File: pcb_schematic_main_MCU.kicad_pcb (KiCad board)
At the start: 2 copper layers, 100.1 x 70.1 mm, 106 parts, among them IC1 LM76202QPWPRQ1, J1 Conn_01x02, J2 Conn_01x03, J3 Conn_01x03_Pin, J4 Conn_01x02, J6 Conn_01x04, P1 USB_C_Plug_USB2.0, Q1 2N3904, Q2 2N3904, U2 TPS62933, U3 USBLC6-2P6, U4 ESP32-S3FN8, U5 SN65HVD232, U6 PC817, U7 PC817, Y1 Crystal_GND24

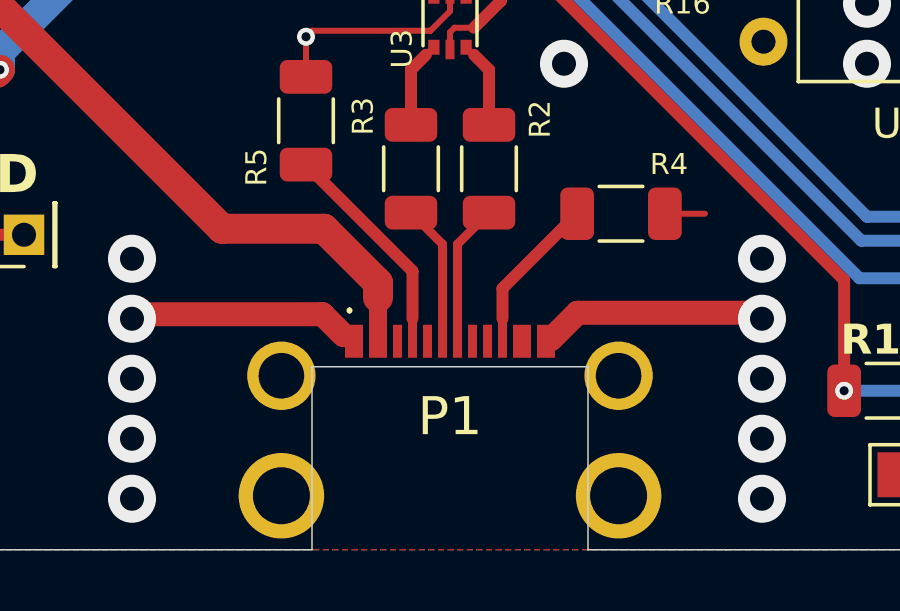
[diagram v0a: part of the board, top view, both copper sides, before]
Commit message: Repair fedback capacitor 3.3V regulator
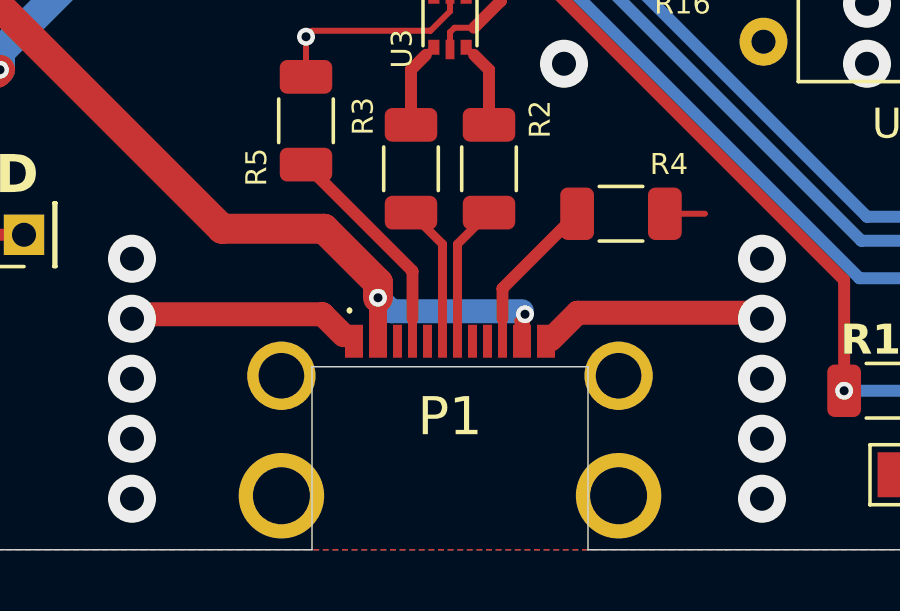
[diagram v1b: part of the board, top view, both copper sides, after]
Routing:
- net /VBUS: track 74.9 -> 83.5 mm, vias 0 -> 2
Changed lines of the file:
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@@
+	)
+	(segment
+		(start 104.85 116.55)
+		(end 104.85 117.25)
+		(width 0.2)
+		(layer "F.Cu")
+		(net 16)
 	)
 	(segment
@@
 	)
 	(segment
+		(start 104.9 116.55)
+		(end 104.85 116.55)
+		(width 0.2)
+		(layer "F.Cu")
+		(net 16)
+	)
+	(segment
+		(start 105.15 116.8)
+		(end 104.9 116.55)
+		(width 0.2)
+		(layer "F.Cu")
+		(net 16)
+	)
+	(segment
+		(start 104.85 117.25)
+		(end 104.85 116.95)
+		(width 0.2)
+		(layer "F.Cu")
+		(net 16)
+	)
+	(segment
 		(start 59.1 86.6)
 		(end 55.15 86.6)
 		(width 1)
+		(layer "F.Cu")
+		(net 16)
+	)
+	(segment
+		(start 105.15 116.4)
+		(end 105.1 116.35)
+		(width 0.2)
 		(layer "F.Cu")
 		(net 16)
@@
 	)
 	(segment
+		(start 105.15 117.25)
+		(end 105.15 116.8)
+		(width 0.2)
+		(layer "F.Cu")
+		(net 16)
+	)
+	(segment
 		(start 100.35 115.95)
 		(end 100.2 115.8)
@@
 	)
 	(segment
+		(start 105.1 116.35)
+		(end 104.9 116.55)
+		(width 0.2)
+		(layer "F.Cu")
+		(net 16)
+	)
+	(segment
+		(start 104.85 116.95)
+		(end 105.15 116.65)
+		(width 0.2)
+		(layer "F.Cu")
+		(net 16)
+	)
+	(segment
 		(start 59.1 86.6)
 		(end 59.1 84.579)
@@
 	)
 	(segment
+		(start 105.15 116.65)
+		(end 105.15 116.4)
+		(width 0.2)
+		(layer "F.Cu")
+		(net 16)
+	)
+	(segment
+		(start 105.15 117.25)
+		(end 105.15 116.65)
+		(width 0.2)
+		(layer "F.Cu")
+		(net 16)
+	)
+	(segment
 		(start 100.2 115.8)
 		(end 100.2 115.3)
@@
 		(net 16)
 	)
+	(via
+		(at 105.1 116.35)
+		(size 0.6)
+		(drill 0.3)
+		(layers "F.Cu" "B.Cu")
+		(net 16)
+	)
+	(via
+		(at 100.2 115.8)
+		(size 0.6)
+		(drill 0.3)
+		(layers "F.Cu" "B.Cu")
+		(net 16)
+	)
+	(segment
+		(start 105 116.25)
+		(end 100.65 116.25)
+		(width 0.8)
+		(layer "B.Cu")
+		(net 16)
+	)
+	(segment
+		(start 105.1 116.35)
+		(end 105 116.25)
+		(width 0.2)
+		(layer "B.Cu")
+		(net 16)
+	)
+	(segment
+		(start 100.65 116.25)
+		(end 100.2 115.8)
+		(width 0.8)
+		(layer "B.Cu")
+		(net 16)
+	)
